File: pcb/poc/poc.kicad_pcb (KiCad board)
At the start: 2 copper layers, 100 x 100 mm, 63 parts, among them J1 USB_B_Mini, J2 Right, J3 Left, J4 AVR-ISP-6, J5 Conn_02x08_Odd_Even, J6 Conn_02x08_Odd_Even, J7 Conn_01x02, J8 Conn_01x02, J9 Conn_02x02_Odd_Even, SW1 SW_Push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

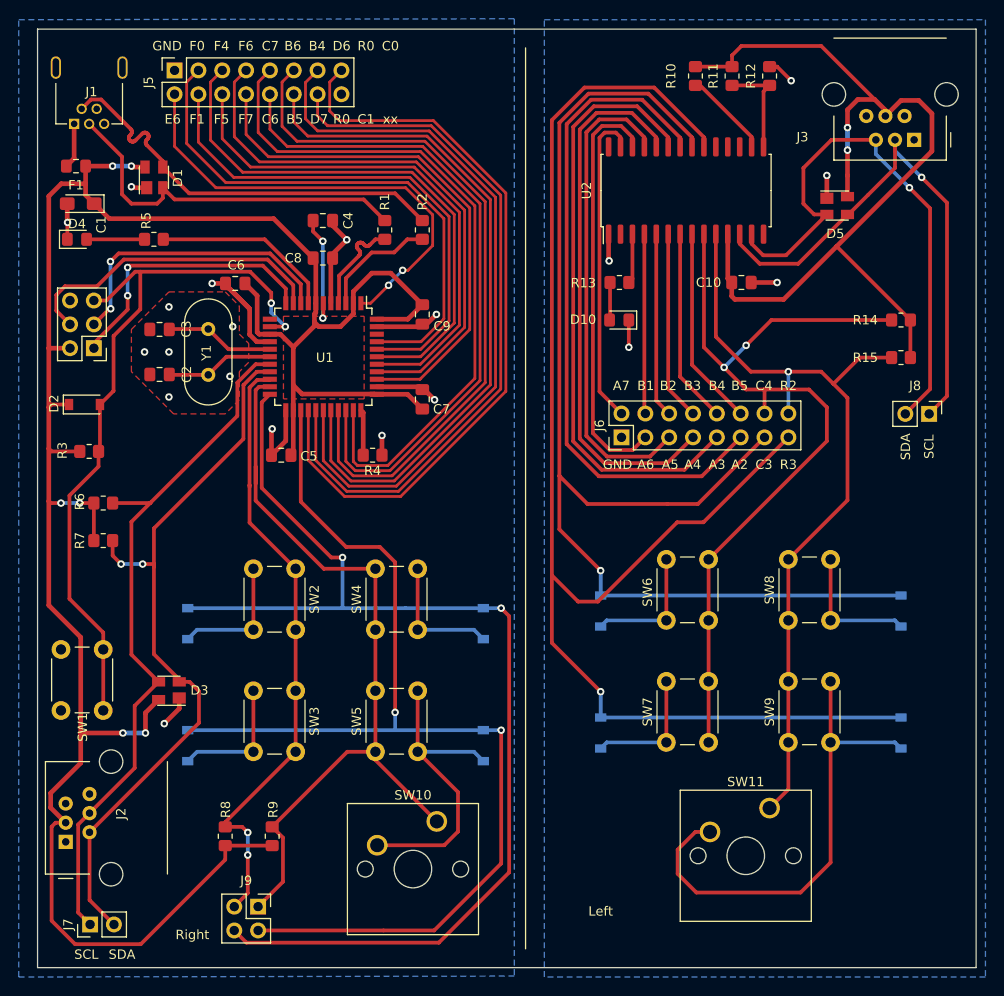
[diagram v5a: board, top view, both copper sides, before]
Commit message: pcb: poc: Silkscreen adjustment
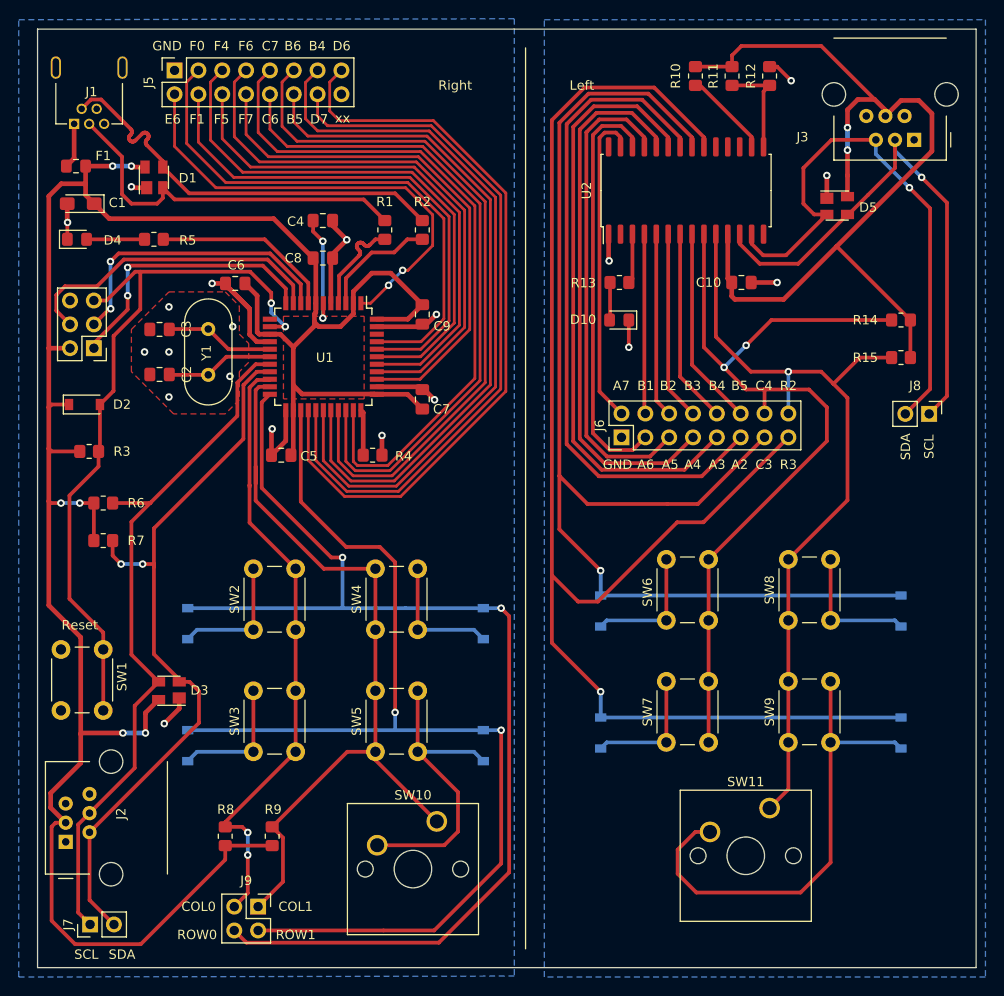
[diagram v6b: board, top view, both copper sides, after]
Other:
- board text added: "COL0"
- board text added: "COL1"
- board text added: "ROW0"
- board text added: "ROW1"
- board text added: "Reset"
- board text removed: "C0"
- board text removed: "C1"
- board text removed: "R0"
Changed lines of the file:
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@@
   (general
     (thickness 1.6)
-    (drawings 47)
+    (drawings 48)
     (tracks 775)
     (zones 0)
@@
     (tags "fuse handsolder")
     (attr smd)
-    (fp_text reference F1 (at 0 -2.02) (layer F.SilkS)
+    (fp_text reference F1 (at -2.905 1.1) (layer F.SilkS)
       (effects (font (size 1 1) (thickness 0.15)))
     )
@@
     (tags SOT-143)
     (attr smd)
-    (fp_text reference D5 (at -0.2 3) (layer F.SilkS)
+    (fp_text reference D5 (at 3.3 0.2) (layer F.SilkS)
       (effects (font (size 1 1) (thickness 0.15)))
     )
@@
     (tags "resistor handsolder")
     (attr smd)
-    (fp_text reference R7 (at -2.5 0 -90) (layer F.SilkS)
+    (fp_text reference R7 (at 3.5 0) (layer F.SilkS)
       (effects (font (size 1 1) (thickness 0.15)))
     )
@@
     (tags "resistor handsolder")
     (attr smd)
-    (fp_text reference R6 (at -2.5 -0.15 -90) (layer F.SilkS)
+    (fp_text reference R6 (at 3.5 0) (layer F.SilkS)
       (effects (font (size 1 1) (thickness 0.15)))
     )
@@
     (tags "capacitor tantalum")
     (attr smd)
-    (fp_text reference C1 (at -2.1875 -2.25 270) (layer F.SilkS)
+    (fp_text reference C1 (at -3.9 0.1) (layer F.SilkS)
       (effects (font (size 1 1) (thickness 0.15)))
     )
@@
     (tags "capacitor handsolder")
     (attr smd)
-    (fp_text reference C4 (at 2.7 0 270) (layer F.SilkS)
+    (fp_text reference C4 (at -2.9 0.1 180) (layer F.SilkS)
       (effects (font (size 1 1) (thickness 0.15)))
     )
@@
     (tags SOT-143)
     (attr smd)
-    (fp_text reference D1 (at -0.07 2.54 90) (layer F.SilkS)
+    (fp_text reference D1 (at -0.07 3.6 180) (layer F.SilkS)
       (effects (font (size 1 1) (thickness 0.15)))
     )
@@
     (tags SOD-123)
     (attr smd)
-    (fp_text reference D2 (at -3.25 -0.1 270) (layer F.SilkS)
+    (fp_text reference D2 (at 4 0) (layer F.SilkS)
       (effects (font (size 1 1) (thickness 0.15)))
     )
@@
     (tags "LED handsolder")
     (attr smd)
-    (fp_text reference D4 (at 0 -1.65) (layer F.SilkS)
+    (fp_text reference D4 (at 3.8 0.1) (layer F.SilkS)
       (effects (font (size 1 1) (thickness 0.15)))
     )
@@
     (tags "resistor handsolder")
     (attr smd)
-    (fp_text reference R1 (at 3 0 90) (layer F.SilkS)
+    (fp_text reference R1 (at 3 0) (layer F.SilkS)
       (effects (font (size 1 1) (thickness 0.15)))
     )
@@
     (tags "resistor handsolder")
     (attr smd)
-    (fp_text reference R2 (at -3 0 90) (layer F.SilkS)
+    (fp_text reference R2 (at -3 0 180) (layer F.SilkS)
       (effects (font (size 1 1) (thickness 0.15)))
     )
@@
     (tags "resistor handsolder")
     (attr smd)
-    (fp_text reference R3 (at -2.85 -0.1 270) (layer F.SilkS)
+    (fp_text reference R3 (at 3.5 0) (layer F.SilkS)
       (effects (font (size 1 1) (thickness 0.15)))
     )
@@
     (tags "resistor handsolder")
     (attr smd)
-    (fp_text reference R4 (at 0 -1.65) (layer F.SilkS)
+    (fp_text reference R4 (at -3.3 -0.1) (layer F.SilkS)
       (effects (font (size 1 1) (thickness 0.15)))
     )
@@
     (tags "resistor handsolder")
     (attr smd)
-    (fp_text reference R5 (at 0.83 2 270) (layer F.SilkS)
+    (fp_text reference R5 (at -3.6 -0.1) (layer F.SilkS)
       (effects (font (size 1 1) (thickness 0.15)))
     )
@@
     (tags "resistor handsolder")
     (attr smd)
-    (fp_text reference R8 (at 2.85 0.05 90) (layer F.SilkS)
+    (fp_text reference R8 (at 2.85 0.05 180) (layer F.SilkS)
       (effects (font (size 1 1) (thickness 0.15)))
     )
@@
     (tags "resistor handsolder")
     (attr smd)
-    (fp_text reference R9 (at 2.85 0.1 90) (layer F.SilkS)
+    (fp_text reference R9 (at 2.85 0.1 180) (layer F.SilkS)
       (effects (font (size 1 1) (thickness 0.15)))
     )
@@
     (tags "resistor handsolder")
     (attr smd)
-    (fp_text reference R10 (at 0 2.6 90) (layer F.SilkS)
+    (fp_text reference R10 (at 0 2.1 90) (layer F.SilkS)
       (effects (font (size 1 1) (thickness 0.15)))
     )
@@
     (descr "tactile push button, 6x6mm e.g. PHAP33xx series, height=4.3mm")
     (tags "tact sw push 6mm")
-    (fp_text reference SW1 (at -1.8 2.31 90) (layer F.SilkS)
+    (fp_text reference SW1 (at 3.6 6.5 90) (layer F.SilkS)
       (effects (font (size 1 1) (thickness 0.15)))
     )
@@
     (descr "tactile push button, 6x6mm e.g. PHAP33xx series, height=4.3mm")
     (tags "tact sw push 6mm")
-    (fp_text reference SW2 (at 3.25 -2 90) (layer F.SilkS)
+    (fp_text reference SW2 (at 3.25 6.5 90) (layer F.SilkS)
       (effects (font (size 1 1) (thickness 0.15)))
     )
@@
     (descr "tactile push button, 6x6mm e.g. PHAP33xx series, height=4.3mm")
     (tags "tact sw push 6mm")
-    (fp_text reference SW3 (at 3.25 -2 90) (layer F.SilkS)
+    (fp_text reference SW3 (at 3.25 6.5 90) (layer F.SilkS)
       (effects (font (size 1 1) (thickness 0.15)))
     )
@@
     )
   )
+  (gr_text COL1 (at 97.5 148.5) (layer F.SilkS)
+    (effects (font (size 1 1) (thickness 0.15)))
+  )
+  (gr_text COL0 (at 89 148.5) (layer F.SilkS)
+    (effects (font (size 1 1) (thickness 0.15)) (justify right))
+  )
+  (gr_text ROW1 (at 97.5 151.5) (layer F.SilkS)
+    (effects (font (size 1 1) (thickness 0.15)))
+  )
+  (gr_text ROW0 (at 87 151.5) (layer F.SilkS)
+    (effects (font (size 1 1) (thickness 0.15)))
+  )
+  (gr_text Reset (at 74.5 118.5) (layer F.SilkS)
+    (effects (font (size 1 1) (thickness 0.15)))
+  )
   (gr_text SDA (at 162.5 99.5 90) (layer F.SilkS)
     (effects (font (size 1 1) (thickness 0.15)))
@@
     (effects (font (size 1 1) (thickness 0.15)))
   )
-  (gr_text xx (at 107.6 64.6) (layer F.SilkS)
-    (effects (font (size 1 1) (thickness 0.15)))
-  )
-  (gr_text C1 (at 105 64.6) (layer F.SilkS)
-    (effects (font (size 1 1) (thickness 0.15)))
-  )
-  (gr_text R0 (at 102.4 64.6) (layer F.SilkS)
+  (gr_text xx (at 102.5 64.5) (layer F.SilkS)
     (effects (font (size 1 1) (thickness 0.15)))
   )
@@
     (effects (font (size 1 1) (thickness 0.15)))
   )
-  (gr_text C0 (at 107.6 56.8) (layer F.SilkS)
-    (effects (font (size 1 1) (thickness 0.15)))
-  )
-  (gr_text R0 (at 105 56.8) (layer F.SilkS)
-    (effects (font (size 1 1) (thickness 0.15)))
-  )
   (gr_text D6 (at 102.4 56.8) (layer F.SilkS)
     (effects (font (size 1 1) (thickness 0.15)))
@@
     (effects (font (size 1 1) (thickness 0.15)))
   )
-  (gr_text Left (at 130 149) (layer F.SilkS)
+  (gr_text Left (at 128 61) (layer F.SilkS)
     (effects (font (size 1 1) (thickness 0.15)))
   )
-  (gr_text Right (at 86.5 151.5) (layer F.SilkS)
+  (gr_text Right (at 114.5 61) (layer F.SilkS)
     (effects (font (size 1 1) (thickness 0.15)))
   )
